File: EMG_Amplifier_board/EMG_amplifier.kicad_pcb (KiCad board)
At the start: 2 copper layers, 5 parts, among them U1 LPV821DBVR

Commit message: add footprints
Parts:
- added C1: 470pF, Capacitor_SMD:C_0805_2012Metric, F.Cu at (164.3, 101.3)
- added C10: 22nF, Capacitor_SMD:C_1210_3225Metric, F.Cu at (164.9, 95.7)
- added C2: 470pF, Capacitor_SMD:C_0805_2012Metric, F.Cu at (168.6, 113.5)
- added C3: 6.8nF, Capacitor_SMD:C_0805_2012Metric, F.Cu at (149.6, 84.4)
- added C4: 33nF, Capacitor_SMD:C_0805_2012Metric, F.Cu at (149.6, 87.4)
- added C9: 10nF, Capacitor_SMD:C_0201_0603Metric, F.Cu at (160.8, 90.0)
- added D1: D_Zener, Diode_SMD:D_SOD-523, F.Cu at (148.9, 102.1)
- added D2: D_Zener, Diode_SMD:D_SOD-523, F.Cu at (148.9, 104.5)
- added D3: D_Zener, Diode_SMD:D_SOD-523, F.Cu at (170.3, 104.0)
- added L1: L_Ferrite, BLM15AX102SN1D_footprints:IND_BLM15_1P05X0P55X0P55_MUR, F.Cu at (145.3, 102.0)
- added L2: L_Ferrite, BLM15AX102SN1D_footprints:IND_BLM15_1P05X0P55X0P55_MUR, F.Cu at (145.3, 104.2)
- added R1: 10kR, Resistor_SMD:R_0805_2012Metric, F.Cu at (145.2, 96.5)
- added R10: 150kR, Resistor_SMD:R_0805_2012Metric, F.Cu at (132.0, 67.5)
- added R11: 150kR, Resistor_SMD:R_0805_2012Metric, F.Cu at (145.2, 82.7)
- added R12: 150kR, Resistor_SMD:R_0805_2012Metric, F.Cu at (145.2, 85.6)
- added R13: 100R, Resistor_SMD:R_0805_2012Metric, F.Cu at (145.2, 88.5)
- added R14: 100R, Resistor_SMD:R_0805_2012Metric, F.Cu at (145.2, 91.5)
- added R15: 12kR, Resistor_SMD:R_0402_1005Metric, F.Cu at (176.5, 78.5)
- added R16: 12kR, Resistor_SMD:R_0402_1005Metric, F.Cu at (187.5, 88.0)
- added R2: 10kR, Resistor_SMD:R_0805_2012Metric, F.Cu at (145.2, 99.4)
- added R22: 27kR, Resistor_SMD:R_0201_0603Metric, F.Cu at (160.8, 91.8)
- added R23: 27kOhm, Resistor_SMD:R_0201_0603Metric, F.Cu at (160.8, 93.5)
- added R3: 2.2kR, Resistor_SMD:R_0603_1608Metric, F.Cu at (149.4, 96.2)
- added R4: 2.2kR, Resistor_SMD:R_0603_1608Metric, F.Cu at (149.4, 98.7)
- added R5: 330R, Resistor_SMD:R_0805_2012Metric, F.Cu at (187.1, 104.0)
- added R6: 10MR, Capacitor_SMD:C_0201_0603Metric, F.Cu at (140.5, 114.5)
- added R7: 10MR, Capacitor_SMD:C_0201_0603Metric, F.Cu at (160.8, 102.5)
- added R8: 10MR, Capacitor_SMD:C_0201_0603Metric, F.Cu at (160.8, 104.2)
- added R9: 10MR, Capacitor_SMD:C_0201_0603Metric, F.Cu at (154.3, 114.5)
- added U1: LPV821DBVR, Components:SOT95P280X145-5N, F.Cu at (165.1, 91.3)
- added U2: INA333xxDGK, Package_SO:VSSOP-8_3x3mm_P0.65mm, F.Cu at (148.4, 73.5)
- added U3: LPV821DBVR, Components:SOT95P280X145-5N, F.Cu at (126.8, 86.0)
- added U5: LPV821DBVR, Components:SOT95P280X145-5N, F.Cu at (161.0, 71.0)
- added U6: LPV821DBVR, Components:SOT95P280X145-5N, F.Cu at (162.7, 84.9)

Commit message: acomponents choice
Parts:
- added U4: TLV8542DR, TLV8542DR_footprints:RUG8_TEX, F.Cu at (172.4, 69.5)
- added U7: TPD2E001DRLR, TPD2E001DRLR_footprints:DRL5-L, F.Cu at (91.0, 86.7)
- C1, C2, C3: footprint Capacitor_SMD:C_0805_2012Metric -> Capacitor_SMD:C_0603_1608Metric
- C10: footprint Capacitor_SMD:C_1210_3225Metric -> Capacitor_SMD:C_0805_2012Metric
- C4: footprint Capacitor_SMD:C_0805_2012Metric -> Capacitor_SMD:C_0201_0603Metric
- C9: footprint Capacitor_SMD:C_0201_0603Metric -> Capacitor_SMD:C_0402_1005Metric
- L1, L2: value L_Ferrite -> L
- R1, R10, R11, R12, R2: footprint Resistor_SMD:R_0805_2012Metric -> Resistor_SMD:R_01005_0402Metric
- R13, R14: footprint Resistor_SMD:R_0805_2012Metric -> Resistor_SMD:R_0201_0603Metric
- R15, R16: footprint Resistor_SMD:R_0402_1005Metric -> Resistor_SMD:R_0201_0603Metric
- R23: value 27kOhm -> 27kR
- R3, R4: footprint Resistor_SMD:R_0603_1608Metric -> Resistor_SMD:R_0402_1005Metric
- R5: footprint Resistor_SMD:R_0805_2012Metric -> Resistor_SMD:R_0402_1005Metric
- R6, R7, R8, R9: footprint Capacitor_SMD:C_0201_0603Metric -> Resistor_SMD:R_0402_1005Metric
- moved R2 84.7 mm to (61.2, 88.0)
- moved R1 84.7 mm to (61.2, 85.5)
- moved R3 82.1 mm to (68.0, 85.5), turned to 180 degrees
- moved L1 82.0 mm to (65.0, 85.5)
- moved L2 82.0 mm to (65.0, 88.0)
- moved R16 65.6 mm to (124.8, 107.5)
- moved D1 22.7 mm to (126.5, 98.0)
- moved R12 22.6 mm to (122.7, 83.0)
- moved U3 22.0 mm to (117.5, 106.0), turned to -90 degrees
- moved R14 14.9 mm to (130.8, 87.5)
- moved R13 8.88 mm to (138.2, 94.0)
- moved C3 6.13 mm to (154.7, 81.0)
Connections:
- R5 pad 1: /output_protection/V_ER -> input_E2

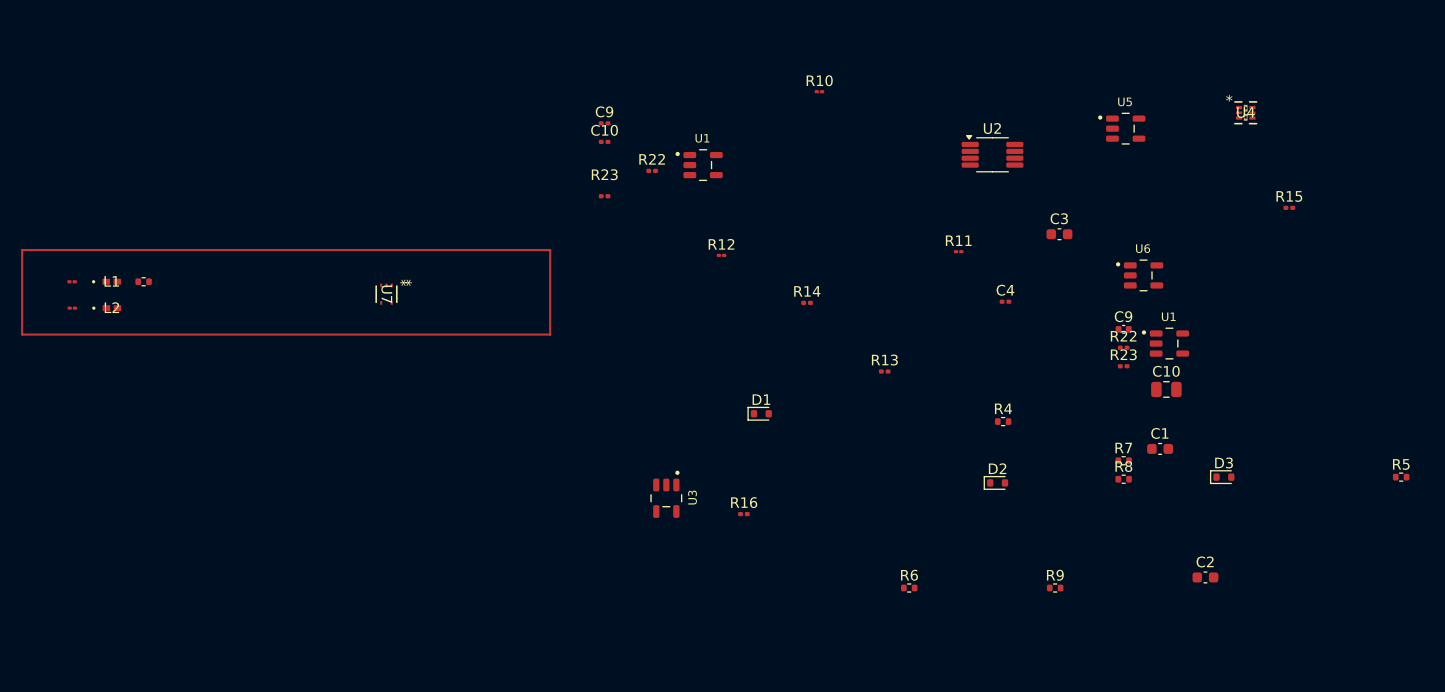
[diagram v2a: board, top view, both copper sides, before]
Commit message: update the schematic with shared grounds and pin connectors
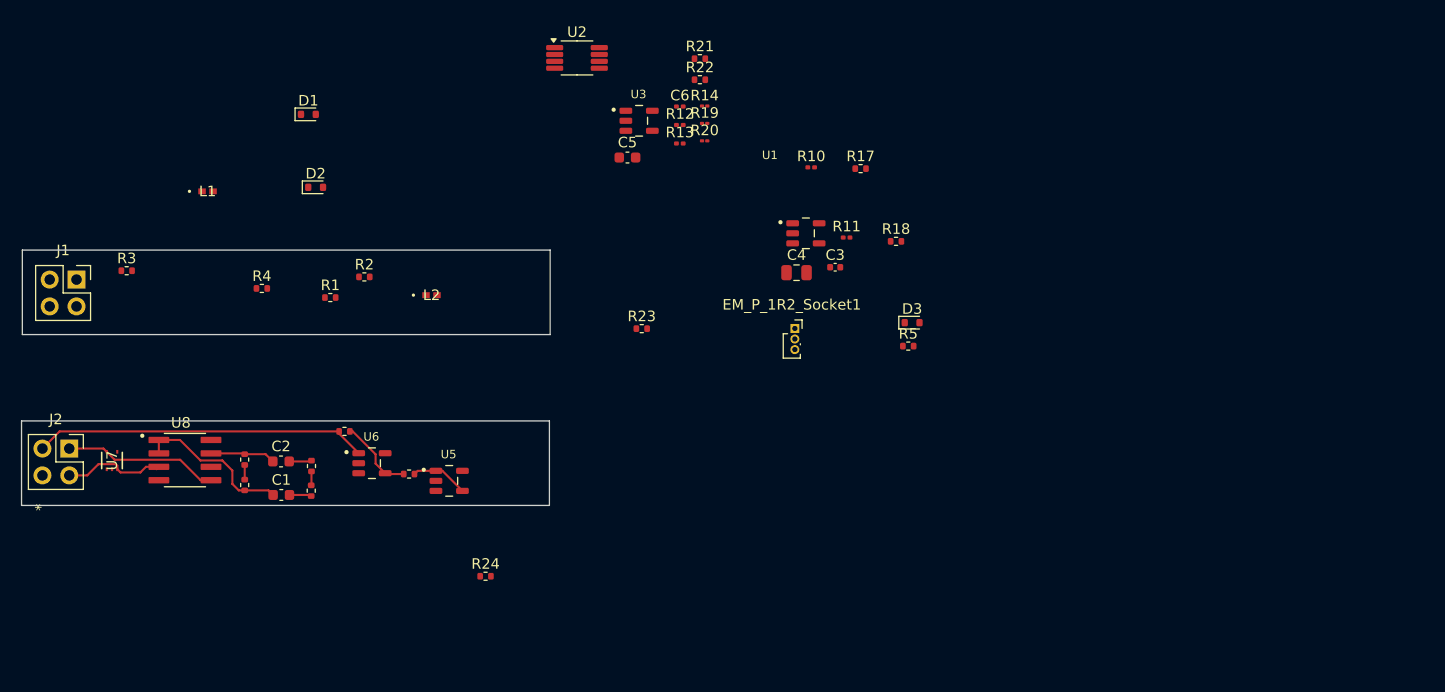
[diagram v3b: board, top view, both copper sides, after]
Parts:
- removed C10: 22nF, Capacitor_SMD:C_0201_0603Metric
- removed C10: 22nF, Capacitor_SMD:C_0805_2012Metric
- removed C9: 10nF, Capacitor_SMD:C_0201_0603Metric
- removed C9: 10nF, Capacitor_SMD:C_0402_1005Metric
- removed the R22 at (116.2, 75.0)
- removed the R22 at (160.8, 91.8)
- removed the R23 at (160.8, 93.5)
- removed the R23 at (111.7, 77.4)
- removed the U1 at (121.0, 74.5)
- removed the U1 at (165.1, 91.3)
- removed U4: TLV8542DR, TLV8542DR_footprints:RUG8_TEX
- added C5: 6.8nF, Capacitor_SMD:C_0603_1608Metric, F.Cu at (113.8, 73.7)
- added C6: 33nF, Capacitor_SMD:C_0201_0603Metric, F.Cu at (118.8, 68.9)
- added EM_P_1R2_Socket1: Conn_01x03_Socket, Connector_PinSocket_1.00mm:PinSocket_1x03_P1.00mm_Vertical, F.Cu at (129.7, 89.9)
- added J1: Conn_01x04_Pin, Connector_PinSocket_2.54mm:PinSocket_2x02_P2.54mm_Vertical, F.Cu at (61.6, 85.3)
- added J2: Conn_01x04_Socket, Connector_PinSocket_2.54mm:PinSocket_2x02_P2.54mm_Vertical, F.Cu at (61.0, 101.3)
- added R17: 10R, Resistor_SMD:R_0402_1005Metric, F.Cu at (135.9, 74.8)
- added R18: 10R, Resistor_SMD:R_0402_1005Metric, F.Cu at (139.2, 81.7)
- added R19: 150kR, Resistor_SMD:R_01005_0402Metric, F.Cu at (121.1, 70.5)
- added R20: 150kR, Resistor_SMD:R_01005_0402Metric, F.Cu at (121.1, 72.2)
- added R21: 10R, Resistor_SMD:R_0402_1005Metric, F.Cu at (120.7, 64.4)
- added R22: 10R, Resistor_SMD:R_0402_1005Metric, F.Cu at (120.7, 66.4)
- added R23: 10R, Resistor_SMD:R_0402_1005Metric, F.Cu at (115.2, 89.9)
- added R24: 10R, Resistor_SMD:R_0402_1005Metric, F.Cu at (100.4, 113.4)
- added U1: LPV821DBVR, Components:SOT95P280X145-5N, F.Cu at (130.7, 80.9)
- added U8: TLV8542DR, TLV8542DR:SOIC127P599X175-8N, F.Cu at (71.9, 102.4)
- C3: value 6.8nF -> 10nF; footprint Capacitor_SMD:C_0603_1608Metric -> Capacitor_SMD:C_0402_1005Metric
- C4: value 33nF -> 22nF; footprint Capacitor_SMD:C_0201_0603Metric -> Capacitor_SMD:C_0805_2012Metric
- L1, L2: value L -> L_Ferrite
- R1, R2: footprint Resistor_SMD:R_01005_0402Metric -> Resistor_SMD:R_0402_1005Metric
- R10, R11: value 150kR -> 27kR; footprint Resistor_SMD:R_01005_0402Metric -> Resistor_SMD:R_0201_0603Metric
- R12: value 150kR -> 100R; footprint Resistor_SMD:R_01005_0402Metric -> Resistor_SMD:R_0201_0603Metric
- R14: value 100R -> 150kR; footprint Resistor_SMD:R_0201_0603Metric -> Resistor_SMD:R_01005_0402Metric
- R15, R16: footprint Resistor_SMD:R_0201_0603Metric -> Resistor_SMD:R_0402_1005Metric
- moved C2 88.2 mm to (81.0, 102.5)
- moved R15 87.1 mm to (93.1, 103.7), turned to 180 degrees
- moved C1 83.3 mm to (81.0, 105.7)
- moved R7 83.2 mm to (77.6, 102.3), turned to 90 degrees
- moved R8 76.9 mm to (83.9, 105.3), turned to 90 degrees
- moved U6 75.2 mm to (89.6, 102.7)
- moved U5 72.2 mm to (96.9, 104.4)
- moved R9 71.4 mm to (83.9, 102.9), turned to 90 degrees
- moved R4 71.3 mm to (79.2, 86.1)
- moved D2 70.4 mm to (84.3, 76.6)
- moved R6 63.7 mm to (77.6, 104.7), turned to 90 degrees
- moved D1 51.4 mm to (83.6, 69.6)
- moved R5 48.3 mm to (140.4, 91.6)
- moved U2 40.4 mm to (109.0, 64.3)
- moved R16 38.6 mm to (87.0, 99.7), turned to 180 degrees
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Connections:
- net /DHPF/V_F1 renamed /Filtering_Board/V_F1
- net /DHPF/V_F2 renamed /Filtering_Board/V_F2
- C3 pad 1: Net-(U2-Ref) -> Net-(U1-IN-)
- C3 pad 2: Net-(U3-IN-) -> GND
- C4 pad 2: GND -> /Processing_Board/V_EMG_OUT
- D3 pad 2: /DRL/V_PR -> /Electrode_Board/V_PR
- R10 pad 1: Net-(R10-Pad1) -> /Processing_Board/LPF_400Hz/V_EMG_INA
- R10 pad 2: /LPF_400Hz/V_EMG_INA -> Net-(C4-Pad1)
- R11 pad 2: Net-(U2-Ref) -> Net-(U1-IN-)
- R12 pad 1: Net-(U3-IN-) -> /Processing_Board/V_CM
- R12 pad 2: Net-(R10-Pad1) -> Net-(R12-Pad2)
- R13 pad 1: /DRL/V_CM -> /Processing_Board/V_CM
- R14 pad 1: /DRL/V_CM -> Net-(U3-IN-)
- R16 pad 2: /DRL/V_PR -> /Filtering_Board/V_PR
- R2 pad 1: input_E2 -> input_ER
- R3 pad 2: /DHPF/V_P1 -> /Electrode_Board/V_I1
- R4 pad 2: /DHPF/V_P2 -> /Electrode_Board/V_I2
- U2 pad 1: Net-(R13-Pad2) -> Net-(R12-Pad2)
- U2 pad 6: /LPF_400Hz/V_EMG_INA -> /Processing_Board/LPF_400Hz/V_EMG_INA
- U2 pad 8: Net-(R14-Pad2) -> Net-(R13-Pad2)
- U3 pad 2: +1V8 -> GND
- U3 pad 3: /first_amp_stage/V_DD/2 -> Net-(U3-IN+)
- U3 pad 5: /first_amp_stage/V_DD -> +1V8
- U5 pad 2: /DRL/V_DD -> GND
- U5 pad 3: /DRL/V_CM -> /Filtering_Board/V_CM
- U5 pad 5: /DRL/+V_DD -> +1V8
- U6 pad 1: /DRL/V_PR -> /Filtering_Board/V_PR
- U6 pad 2: /DRL/V_DD -> GND
- U6 pad 3: /DRL/V_DD/2 -> Net-(U6-IN+)
- U6 pad 5: /DRL/+V_DD -> +1V8
- U7 pad 1: GND -> +1V8
- U7 pad 2: GND -> unconnected-(U7-NC-Pad2)
- U7 pad 3: /DHPF/V_P2 -> /Filtering_Board/V_I1
- U7 pad 5: /DHPF/V_P1 -> /Filtering_Board/V_I2
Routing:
- net /Filtering_Board/V_PR: track 0.00 -> 31.6 mm
- net Net-(U8--INA): track 0.00 -> 15.0 mm
- net /Filtering_Board/V_I2: track 0.00 -> 14.7 mm
- net /Filtering_Board/V_I1: track 0.00 -> 9.98 mm
- net Net-(U6-IN-): track 0.00 -> 7.29 mm
- net Net-(U8--INB): track 0.00 -> 6.17 mm
- net Net-(U5-IN-): track 0.00 -> 5.46 mm
- net Net-(R6-Pad2): track 0.00 -> 2.72 mm
- net /Filtering_Board/V_F2: track 0.00 -> 2.14 mm
- net /Filtering_Board/V_F1: track 0.00 -> 2.10 mm
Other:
- board outline added: 50.1 x 24.2 mm

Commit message: pcb design v1
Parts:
- removed EM_P_1R2_Socket1: Conn_01x03_Socket, Connector_PinSocket_1.00mm:PinSocket_1x03_P1.00mm_Vertical
- removed R17, R18: 10R, Resistor_SMD:R_0402_1005Metric
- added C10: 0.1uF, Capacitor_SMD:C_0805_2012Metric, B.Cu at (76.6, 117.9)
- added C11: 0.1uF, Capacitor_SMD:C_0805_2012Metric, B.Cu at (94.4, 119.8)
- added C12: 0.1uF, Capacitor_SMD:C_0805_2012Metric, B.Cu at (87.2, 100.3)
- added C7: 0.1uF, Capacitor_SMD:C_0805_2012Metric, B.Cu at (77.6, 101.2)
- added C8: 0.1uF, Capacitor_SMD:C_0805_2012Metric, B.Cu at (95.9, 103.0)
- added C9: 0.1uF, Capacitor_SMD:C_0805_2012Metric, F.Cu at (72.8, 109.4)
- added J3: Conn_01x06_Pin, Connector_PinHeader_2.54mm:PinHeader_2x03_P2.54mm_Vertical, B.Cu at (104.1, 119.6)
- added J4: Conn_01x06_Socket, Connector_PinSocket_2.54mm:PinSocket_2x03_P2.54mm_Vertical, F.Cu at (103.9, 103.9)
- added J5: Conn_01x04_Pin, Connector_PinHeader_2.54mm:PinHeader_2x02_P2.54mm_Vertical, F.Cu at (61.6, 119.7)
- added J6: Conn_01x01_Pin, Connector_PinHeader_2.54mm:PinHeader_1x01_P2.54mm_Vertical, F.Cu at (65.2, 119.7)
- C6: footprint Capacitor_SMD:C_0201_0603Metric -> Capacitor_SMD:C_0805_2012Metric
- J1: value Conn_01x04_Pin -> Conn_01x04_Socket
- J2: value Conn_01x04_Socket -> Conn_01x04_Pin; moved to B.Cu
- R10, R11, R12, R13: footprint Resistor_SMD:R_0201_0603Metric -> Resistor_SMD:R_0402_1005Metric
- R14, R19, R20: footprint Resistor_SMD:R_01005_0402Metric -> Resistor_SMD:R_0402_1005Metric
- R21, R22: value 10R -> 10k
- R23, R24: value 10R -> 10k; moved to B.Cu
- moved R10 71.9 mm to (75.2, 119.8), turned to 180 degrees
- moved U1 71.0 mm to (69.6, 117.0)
- moved R11 70.1 mm to (74.7, 117.9), turned to 90 degrees
- moved R21 68.8 mm to (75.2, 116.0)
- moved C4 67.6 mm to (72.1, 119.8), turned to 180 degrees
- moved R22 67.3 mm to (77.5, 117.9), turned to -90 degrees
- moved C3 66.7 mm to (76.0, 117.9), turned to -90 degrees
- moved R14 63.9 mm to (79.5, 117.3), turned to -90 degrees
- moved R20 63.0 mm to (79.5, 119.4), turned to -90 degrees
- moved R19 60.6 mm to (86.4, 120.2), turned to 180 degrees
- moved D3 59.5 mm to (81.5, 84.6), turned to 180 degrees
- moved C6 58.5 mm to (88.8, 119.2), turned to -90 degrees
- moved U3 57.4 mm to (82.8, 117.8), turned to 180 degrees
- moved R5 55.6 mm to (85.2, 85.1), turned to 90 degrees
- moved U2 55.3 mm to (93.1, 117.2), turned to 180 degrees
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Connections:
- J1 pad 1: /Electrode_Board/V_I2 -> GND
- J1 pad 2: /Electrode_Board/V_PR -> /Electrode_Board/V_I1
- J1 pad 3: /Electrode_Board/V_I1 -> /Electrode_Board/V_PR
- J1 pad 4: GND -> /Electrode_Board/V_I2
- J2 pad 1: /Filtering_Board/V_I2 -> GND
- J2 pad 2: /Filtering_Board/V_PR -> /Filtering_Board/V_I1
- J2 pad 3: /Filtering_Board/V_I1 -> /Filtering_Board/V_PR
- J2 pad 4: GND -> /Filtering_Board/V_I2
- R2 pad 1: input_ER -> input_E2
- R23 pad 1: +1V8 -> /Filtering_Board/+V_DD
- R5 pad 1: input_E2 -> input_ER
- U2 pad 2: /Filtering_Board/V_F2 -> /Processing_Board/V_F2
- U2 pad 3: /Filtering_Board/V_F1 -> /Processing_Board/V_F1
- U2 pad 4: unconnected-(U2-V--Pad4) -> GND
- U2 pad 7: unconnected-(U2-V+-Pad7) -> +1V8
- U5 pad 5: +1V8 -> /Filtering_Board/+V_DD
- U6 pad 5: +1V8 -> /Filtering_Board/+V_DD
- U7 pad 1: +1V8 -> /Filtering_Board/+V_DD
- U8 pad 8: +1V8 -> /Filtering_Board/+V_DD
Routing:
- net +1V8: track 0.00 -> 85.4 mm, vias 0 -> 5
- net /Filtering_Board/+V_DD: track 0.00 -> 74.8 mm, vias 0 -> 8
- net GND: track 0.00 -> 59.8 mm, vias 0 -> 19
- net /Electrode_Board/V_I1: track 0.00 -> 33.6 mm
- net /Electrode_Board/V_PR: track 0.00 -> 25.3 mm
- net /Filtering_Board/V_F1: track 2.10 -> 25.5 mm
- net /Filtering_Board/V_F2: track 2.14 -> 24.7 mm
- net /Processing_Board/LPF_400Hz/V_EMG_INA: track 0.00 -> 16.5 mm
- net /Processing_Board/V_EMG_OUT: track 0.00 -> 14.6 mm
- net /Filtering_Board/V_CM: track 0.00 -> 12.5 mm, vias 0 -> 2
- net /Processing_Board/V_CM: track 0.00 -> 12.5 mm
- net Net-(U2-Ref): track 0.00 -> 11.1 mm, vias 0 -> 3
- net Net-(U3-IN+): track 0.00 -> 11.0 mm, vias 0 -> 2
- net /Processing_Board/V_F1: track 0.00 -> 10.3 mm
- net Net-(U3-IN-): track 0.00 -> 8.79 mm
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- added copper zone on B.Cu, net GND
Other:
- board size 50.1 x 24.2 mm -> 50.1 x 39.8 mm
